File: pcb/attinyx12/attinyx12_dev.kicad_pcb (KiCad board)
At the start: 2 copper layers, 22.6 x 52 mm, 24 parts, among them J1 USB_C_Receptacle_USB2.0_16P, J2 Conn_01x04, J3 Conn_01x04, J4 Conn_02x06, U1 USBLC6-2SC6, U2 ATtiny212-SS, U3 CH342K

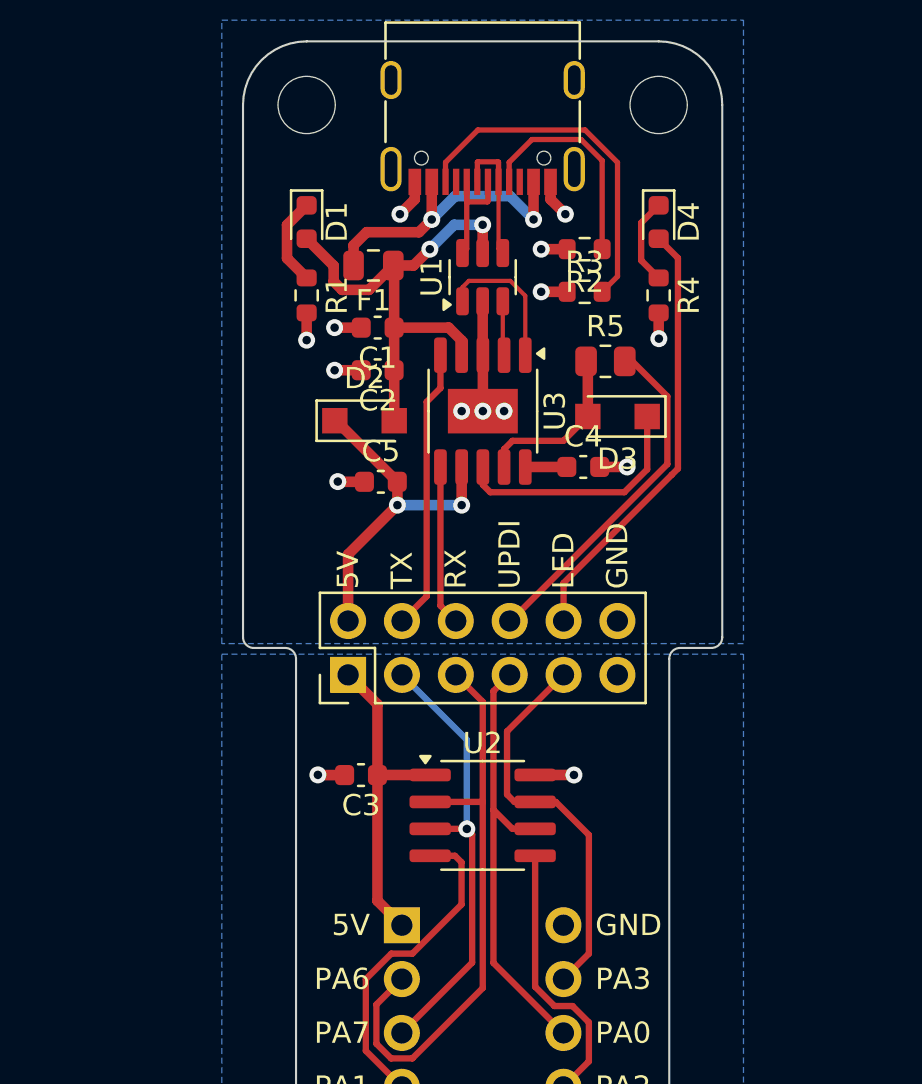
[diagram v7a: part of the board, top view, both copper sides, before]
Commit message: rearrange layout
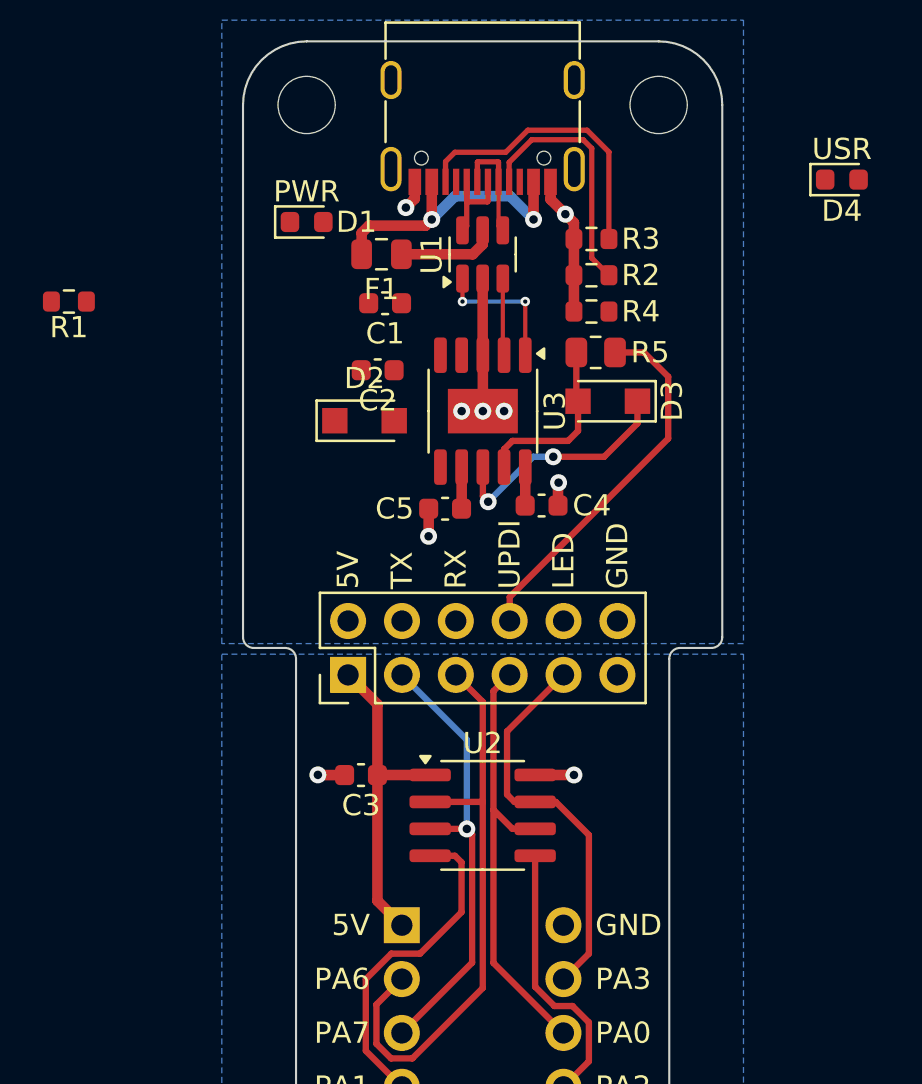
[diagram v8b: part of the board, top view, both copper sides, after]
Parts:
- moved R1 11.2 mm to (60.5, 39.4), turned to 0 degrees
- moved D4 8.87 mm to (96.9, 33.6), turned to 0 degrees
- moved C5 3.29 mm to (78.2, 49.1)
- moved R4 3.26 mm to (85.1, 39.8), turned to 180 degrees
- moved C4 2.68 mm to (82.8, 49.0)
- moved R3 2.51 mm to (85.1, 36.4)
- moved R2 1.27 mm to (85.1, 38.1)
- moved C1 1.20 mm to (75.4, 39.5)
- moved U1 1.07 mm to (80.0, 37.1)
- moved D3 0.85 mm to (85.9, 44.1)
- moved F1 0.65 mm to (75.2, 37.1)
- moved R5 0.62 mm to (85.3, 41.8)
- turned D1 to 0 degrees
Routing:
- net /LED: track 20.6 -> 0.00 mm
- net VBUS: track 23.8 -> 4.69 mm, vias 2 -> 0
- net +5V: track 16.5 -> 1.97 mm, vias 2 -> 0
- net /TX: track 13.3 -> 0.00 mm
- net /RX: track 7.56 -> 0.00 mm
- net Net-(D1-K): track 4.19 -> 0.00 mm
- net Net-(D4-K): track 4.11 -> 0.00 mm
- net Net-(J1-CC2): track 16.7 -> 13.9 mm
- net GND: track 18.8 -> 16.6 mm, vias 13 -> 7
- net Net-(J1-CC1): track 10.3 -> 11.7 mm
- net /UPDI: track 16.4 -> 17.6 mm
- net /UD-: track 2.57 -> 3.64 mm
- net /D-: track 6.30 -> 5.23 mm
- net /D+: track 6.30 -> 5.23 mm
- net Net-(F1-Pad1): track 14.4 -> 13.8 mm
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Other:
- board text added: "PWR"
- board text added: "USR"
